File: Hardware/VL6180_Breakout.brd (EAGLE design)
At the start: 44.5 x 13 mm, 24 parts, among them U1 VL6180, U3 MIC5219 3.3V

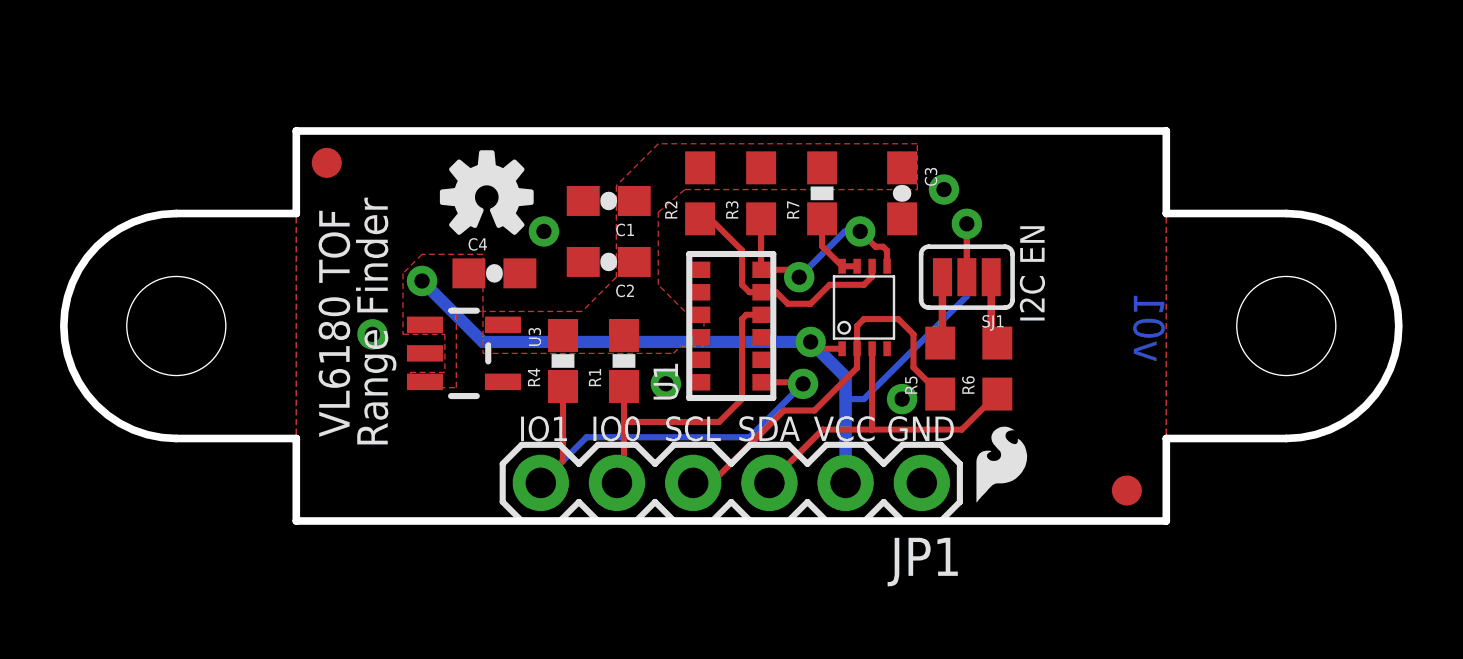
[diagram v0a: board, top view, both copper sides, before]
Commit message: finished layout and added simple breakout board layout
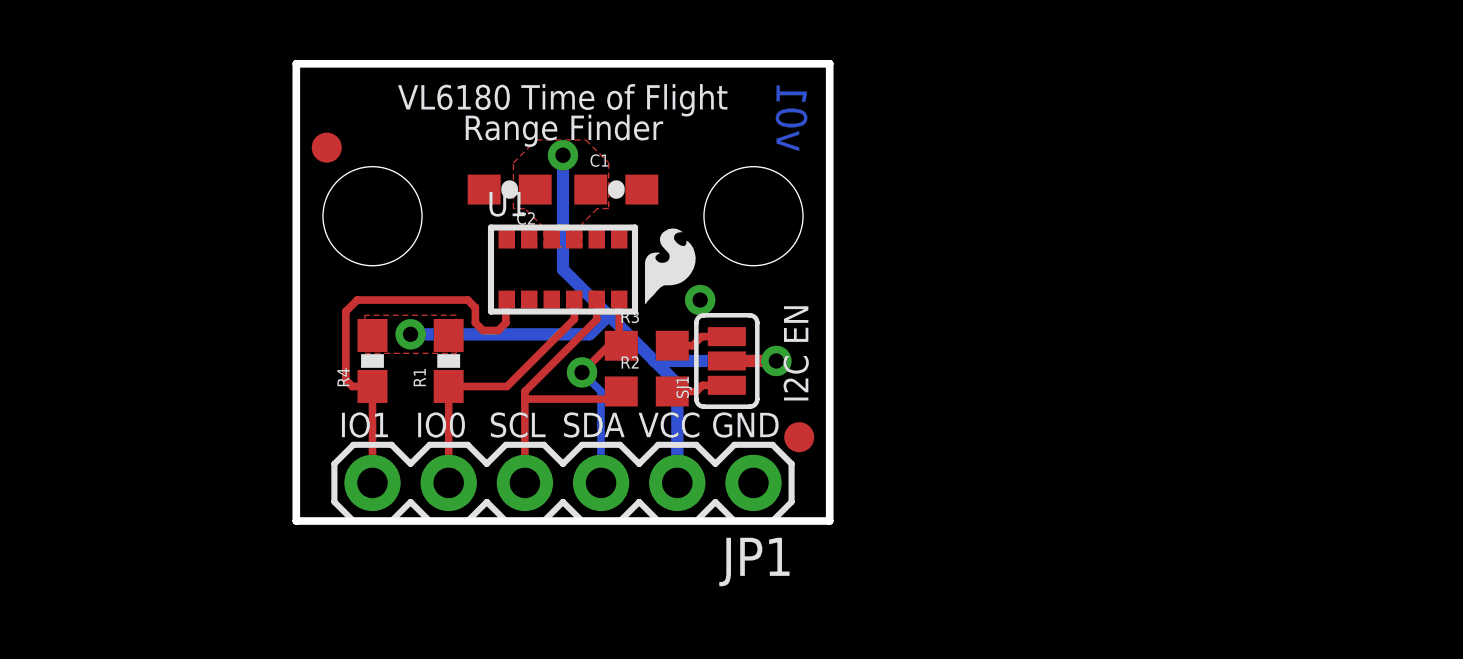
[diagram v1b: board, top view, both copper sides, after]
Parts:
- removed C3, C4: 0.1uF, SparkFun-Capacitors:0603-CAP
- removed R5, R6: 4.7k, SparkFun-Resistors:0603
- removed R7: 200k, SparkFun-Resistors:0603-RES
- removed U2: (no value), SparkFun-DigitalIC:PSOP-8
- removed U3: MIC5219 3.3V, SparkFun-PowerIC:SOT23-5
- moved FID2 29.0 mm to (1.02, 12.4)
- moved LOGO1 20.9 mm to (3.17, 15.0), turned to 180 degrees
- moved FID1 18.2 mm to (16.8, 2.79)
- moved STANDOFF2 18.1 mm to (15.2, 10.2)
- moved U$2 12.9 mm to (11.3, 6.86)
- moved SJ1 8.47 mm to (14.4, 5.33), turned to 90 degrees
- moved STANDOFF1 7.49 mm to (2.54, 10.2)
- moved R2 6.84 mm to (11.7, 4.32), turned to 0 degrees
- moved R3 6.35 mm to (11.7, 5.84), turned to 0 degrees
- moved R4 6.35 mm to (2.54, 5.33)
- moved U1 5.92 mm to (8.89, 8.38), turned to 0 degrees
- moved R1 5.84 mm to (5.08, 5.33)
- moved JP1 5.61 mm to (15.2, 1.27)
- moved C2 4.09 mm to (7.11, 11.0)
- moved LOGO2 3.17 mm to (8.89, 8.89), flipped to the bottom, turned to 180 degrees
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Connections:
- removed net N$3: R5.2, SJ1.3
- removed net SCL_LV: R2.1, U1.5, U2.6
- removed net SDA_LV: R3.1, U1.6, U2.5
- removed net VCC: C4.1, JP1.2, SJ1.2, U2.1, U3.1, U3.3
- net 2.8V: now also JP1.2, SJ1.2; no longer C3.1, R2.2, R3.2, R7.2, U3.5
- net GND: no longer C3.2, C4.2, U2.4, U3.2
- net N$1: now also R2.2, SJ1.1; no longer R7.1, U2.7, U2.8
- net N$2: now also R3.2, SJ1.3; no longer R6.2, SJ1.1
- net SCL: now also R2.1, U1.5; no longer R5.1, U2.2
- net SDA: now also R3.1, U1.6; no longer R6.1, U2.3
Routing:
- net VCC: track 29.8 -> 0.00 mm, vias 3 -> 0
- net 2.8V: track 0.00 -> 25.1 mm, vias 0 -> 3
- net SCL_LV: track 8.30 -> 0.00 mm
- net SDA_LV: track 7.41 -> 0.00 mm, vias 2 -> 0
- net SDA: track 11.5 -> 7.16 mm, vias 0 -> 1
- net SCL: track 13.0 -> 10.4 mm
- net N$3: track 2.21 -> 0.00 mm
- net GPIO0: track 10.9 -> 8.99 mm
- net GPIO1: track 15.0 -> 13.6 mm, vias 1 -> 0
- removed copper zone on layer 1, net VCC
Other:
- board size 44.5 x 13 mm -> 17.8 x 15.2 mm
- board text added: "VL6180 Time of Flight"
- board text removed: "Vl6180 Time of Flight Range Finder"
